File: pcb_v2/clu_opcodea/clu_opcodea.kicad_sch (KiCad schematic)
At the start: 45 parts, among them J1 UCODE, U1 74LS00

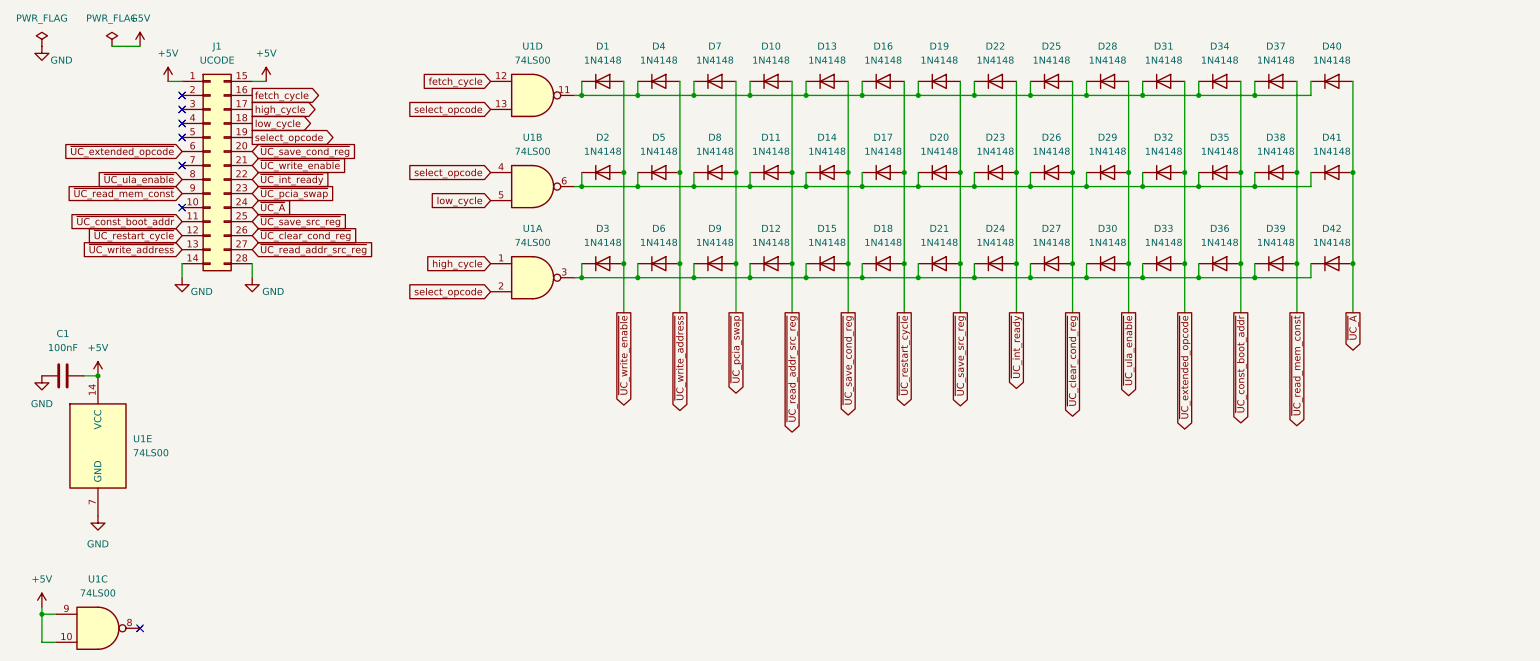
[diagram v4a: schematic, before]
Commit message: ajuste nos sinais do microcódigo
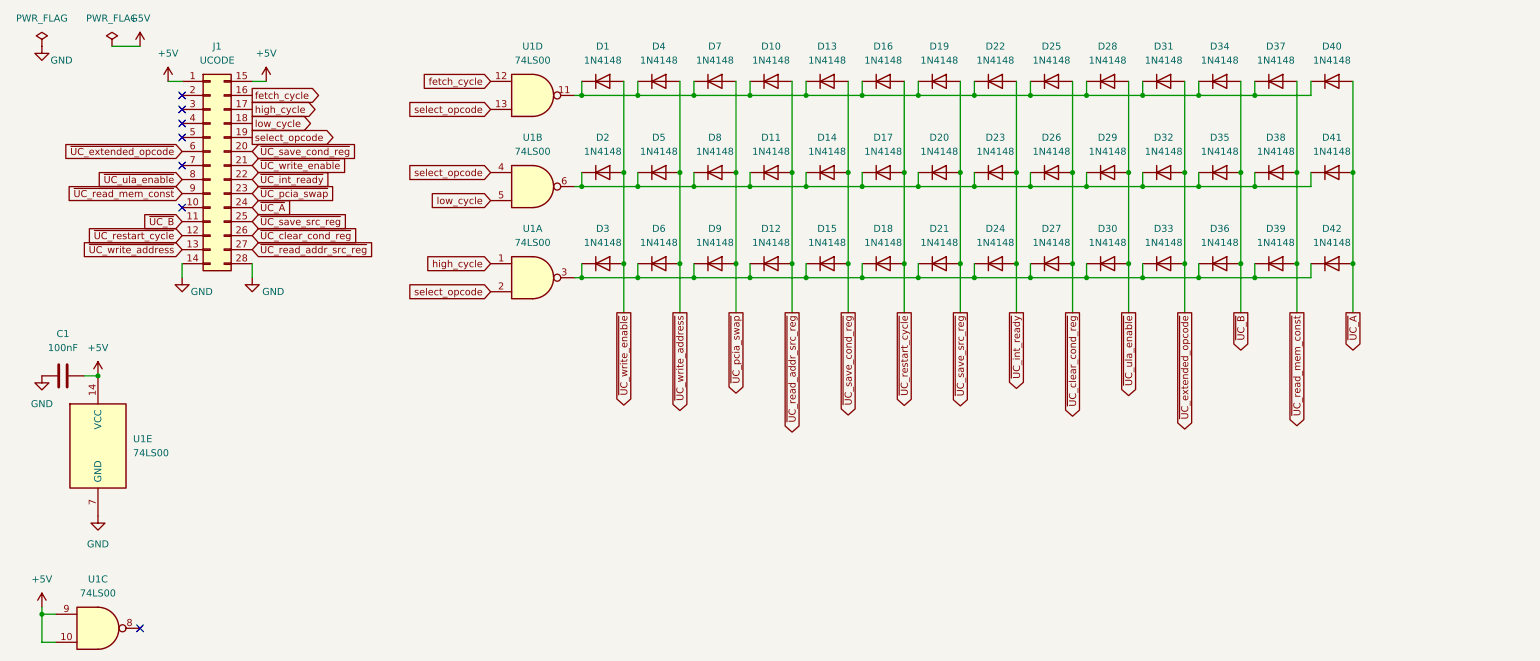
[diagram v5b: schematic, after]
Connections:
- net ~{UC_const_boot_addr} renamed ~{UC_B}
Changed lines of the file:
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@@
 		)
 	)
-	(global_label "~{UC_const_boot_addr}"
+	(global_label "~{UC_read_mem_const}"
+		(shape output)
+		(at 247.65 69.85 270)
+		(fields_autoplaced yes)
+		(effects
+			(font
+				(size 1.27 1.27)
+			)
+			(justify right)
+		)
+		(property "Intersheetrefs" "${INTERSHEET_REFS}"
+			(at 247.65 92.1269 90)
+			(effects
+				(font
+					(size 1.27 1.27)
+				)
+				(justify right)
+				(hide yes)
+			)
+		)
+	)
+	(global_label "~{UC_write_address}"
+		(shape output)
+		(at 135.89 69.85 270)
+		(fields_autoplaced yes)
+		(effects
+			(font
+				(size 1.27 1.27)
+			)
+			(justify right)
+		)
+		(property "Intersheetrefs" "${INTERSHEET_REFS}"
+			(at 135.89 89.2847 90)
+			(effects
+				(font
+					(size 1.27 1.27)
+				)
+				(justify right)
+				(hide yes)
+			)
+		)
+	)
+	(global_label "~{UC_clear_cond_reg}"
+		(shape input)
+		(at 58.42 55.88 0)
+		(fields_autoplaced yes)
+		(effects
+			(font
+				(size 1.27 1.27)
+			)
+			(justify left)
+		)
+		(property "Intersheetrefs" "${INTERSHEET_REFS}"
+			(at 79.2455 55.88 0)
+			(effects
+				(font
+					(size 1.27 1.27)
+				)
+				(justify left)
+				(hide yes)
+			)
+		)
+	)
+	(global_label "~{UC_extended_opcode}"
+		(shape input)
+		(at 45.72 40.64 180)
+		(fields_autoplaced yes)
+		(effects
+			(font
+				(size 1.27 1.27)
+			)
+			(justify right)
+		)
+		(property "Intersheetrefs" "${INTERSHEET_REFS}"
+			(at 22.9593 40.64 0)
+			(effects
+				(font
+					(size 1.27 1.27)
+				)
+				(justify right)
+				(hide yes)
+			)
+		)
+	)
+	(global_label "high_cycle"
+		(shape input)
+		(at 101.6 60.96 180)
+		(fields_autoplaced yes)
+		(effects
+			(font
+				(size 1.27 1.27)
+			)
+			(justify right)
+		)
+		(property "Intersheetrefs" "${INTERSHEET_REFS}"
+			(at 88.6968 60.96 0)
+			(effects
+				(font
+					(size 1.27 1.27)
+				)
+				(justify right)
+				(hide yes)
+			)
+		)
+	)
+	(global_label "~{UC_A}"
+		(shape input)
+		(at 58.42 50.8 0)
+		(fields_autoplaced yes)
+		(effects
+			(font
+				(size 1.27 1.27)
+			)
+			(justify left)
+		)
+		(property "Intersheetrefs" "${INTERSHEET_REFS}"
+			(at 66.0619 50.8 0)
+			(effects
+				(font
+					(size 1.27 1.27)
+				)
+				(justify left)
+				(hide yes)
+			)
+		)
+	)
+	(global_label "~{UC_pcia_swap}"
+		(shape input)
+		(at 58.42 48.26 0)
+		(fields_autoplaced yes)
+		(effects
+			(font
+				(size 1.27 1.27)
+			)
+			(justify left)
+		)
+		(property "Intersheetrefs" "${INTERSHEET_REFS}"
+			(at 74.5889 48.26 0)
+			(effects
+				(font
+					(size 1.27 1.27)
+				)
+				(justify left)
+				(hide yes)
+			)
+		)
+	)
+	(global_label "~{UC_B}"
+		(shape input)
+		(at 45.72 53.34 180)
+		(fields_autoplaced yes)
+		(effects
+			(font
+				(size 1.27 1.27)
+			)
+			(justify right)
+		)
+		(property "Intersheetrefs" "${INTERSHEET_REFS}"
+			(at 37.8967 53.34 0)
+			(effects
+				(font
+					(size 1.27 1.27)
+				)
+				(justify right)
+				(hide yes)
+			)
+		)
+	)
+	(global_label "~{UC_A}"
+		(shape output)
+		(at 257.81 69.85 270)
+		(fields_autoplaced yes)
+		(effects
+			(font
+				(size 1.27 1.27)
+			)
+			(justify right)
+		)
+		(property "Intersheetrefs" "${INTERSHEET_REFS}"
+			(at 257.81 77.4919 90)
+			(effects
+				(font
+					(size 1.27 1.27)
+				)
+				(justify right)
+				(hide yes)
+			)
+		)
+	)
+	(global_label "~{UC_int_ready}"
+		(shape output)
+		(at 196.85 69.85 270)
+		(fields_autoplaced yes)
+		(effects
+			(font
+				(size 1.27 1.27)
+			)
+			(justify right)
+		)
+		(property "Intersheetrefs" "${INTERSHEET_REFS}"
+			(at 196.85 84.9908 90)
+			(effects
+				(font
+					(size 1.27 1.27)
+				)
+				(justify right)
+				(hide yes)
+			)
+		)
+	)
+	(global_label "~{UC_extended_opcode}"
+		(shape output)
+		(at 227.33 69.85 270)
+		(fields_autoplaced yes)
+		(effects
+			(font
+				(size 1.27 1.27)
+			)
+			(justify right)
+		)
+		(property "Intersheetrefs" "${INTERSHEET_REFS}"
+			(at 227.33 92.6107 90)
+			(effects
+				(font
+					(size 1.27 1.27)
+				)
+				(justify right)
+				(hide yes)
+			)
+		)
+	)
+	(global_label "~{UC_B}"
 		(shape output)
 		(at 237.49 69.85 270)
@@
 		)
 		(property "Intersheetrefs" "${INTERSHEET_REFS}"
-			(at 237.49 91.8848 90)
-			(effects
-				(font
-					(size 1.27 1.27)
-				)
-				(justify right)
-				(hide yes)
-			)
-		)
-	)
-	(global_label "~{UC_read_mem_const}"
-		(shape output)
-		(at 247.65 69.85 270)
-		(fields_autoplaced yes)
-		(effects
-			(font
-				(size 1.27 1.27)
-			)
-			(justify right)
-		)
-		(property "Intersheetrefs" "${INTERSHEET_REFS}"
-			(at 247.65 92.1269 90)
-			(effects
-				(font
-					(size 1.27 1.27)
-				)
-				(justify right)
-				(hide yes)
-			)
-		)
-	)
-	(global_label "~{UC_write_address}"
-		(shape output)
-		(at 135.89 69.85 270)
-		(fields_autoplaced yes)
-		(effects
-			(font
-				(size 1.27 1.27)
-			)
-			(justify right)
-		)
-		(property "Intersheetrefs" "${INTERSHEET_REFS}"
-			(at 135.89 89.2847 90)
-			(effects
-				(font
-					(size 1.27 1.27)
-				)
-				(justify right)
-				(hide yes)
-			)
-		)
-	)
-	(global_label "~{UC_clear_cond_reg}"
-		(shape input)
-		(at 58.42 55.88 0)
-		(fields_autoplaced yes)
-		(effects
-			(font
-				(size 1.27 1.27)
-			)
-			(justify left)
-		)
-		(property "Intersheetrefs" "${INTERSHEET_REFS}"
-			(at 79.2455 55.88 0)
-			(effects
-				(font
-					(size 1.27 1.27)
-				)
-				(justify left)
-				(hide yes)
-			)
-		)
-	)
-	(global_label "~{UC_extended_opcode}"
-		(shape input)
-		(at 45.72 40.64 180)
-		(fields_autoplaced yes)
-		(effects
-			(font
-				(size 1.27 1.27)
-			)
-			(justify right)
-		)
-		(property "Intersheetrefs" "${INTERSHEET_REFS}"
-			(at 22.9593 40.64 0)
-			(effects
-				(font
-					(size 1.27 1.27)
-				)
-				(justify right)
-				(hide yes)
-			)
-		)
-	)
-	(global_label "high_cycle"
-		(shape input)
-		(at 101.6 60.96 180)
-		(fields_autoplaced yes)
-		(effects
-			(font
-				(size 1.27 1.27)
-			)
-			(justify right)
-		)
-		(property "Intersheetrefs" "${INTERSHEET_REFS}"
-			(at 88.6968 60.96 0)
-			(effects
-				(font
-					(size 1.27 1.27)
-				)
-				(justify right)
-				(hide yes)
-			)
-		)
-	)
-	(global_label "~{UC_A}"
-		(shape input)
-		(at 58.42 50.8 0)
-		(fields_autoplaced yes)
-		(effects
-			(font
-				(size 1.27 1.27)
-			)
-			(justify left)
-		)
-		(property "Intersheetrefs" "${INTERSHEET_REFS}"
-			(at 66.0619 50.8 0)
-			(effects
-				(font
-					(size 1.27 1.27)
-				)
-				(justify left)
-				(hide yes)
-			)
-		)
-	)
-	(global_label "~{UC_pcia_swap}"
-		(shape input)
-		(at 58.42 48.26 0)
-		(fields_autoplaced yes)
-		(effects
-			(font
-				(size 1.27 1.27)
-			)
-			(justify left)
-		)
-		(property "Intersheetrefs" "${INTERSHEET_REFS}"
-			(at 74.5889 48.26 0)
-			(effects
-				(font
-					(size 1.27 1.27)
-				)
-				(justify left)
-				(hide yes)
-			)
-		)
-	)
-	(global_label "~{UC_A}"
-		(shape output)
-		(at 257.81 69.85 270)
-		(fields_autoplaced yes)
-		(effects
-			(font
-				(size 1.27 1.27)
-			)
-			(justify right)
-		)
-		(property "Intersheetrefs" "${INTERSHEET_REFS}"
-			(at 257.81 77.4919 90)
-			(effects
-				(font
-					(size 1.27 1.27)
-				)
-				(justify right)
-				(hide yes)
-			)
-		)
-	)
-	(global_label "~{UC_int_ready}"
-		(shape output)
-		(at 196.85 69.85 270)
-		(fields_autoplaced yes)
-		(effects
-			(font
-				(size 1.27 1.27)
-			)
-			(justify right)
-		)
-		(property "Intersheetrefs" "${INTERSHEET_REFS}"
-			(at 196.85 84.9908 90)
-			(effects
-				(font
-					(size 1.27 1.27)
-				)
-				(justify right)
-				(hide yes)
-			)
-		)
-	)
-	(global_label "~{UC_extended_opcode}"
-		(shape output)
-		(at 227.33 69.85 270)
-		(fields_autoplaced yes)
-		(effects
-			(font
-				(size 1.27 1.27)
-			)
-			(justify right)
-		)
-		(property "Intersheetrefs" "${INTERSHEET_REFS}"
-			(at 227.33 92.6107 90)
-			(effects
-				(font
-					(size 1.27 1.27)
-				)
-				(justify right)
-				(hide yes)
-			)
-		)
-	)
-	(global_label "~{UC_const_boot_addr}"
-		(shape input)
-		(at 45.72 53.34 180)
-		(fields_autoplaced yes)
-		(effects
-			(font
-				(size 1.27 1.27)
-			)
-			(justify right)
-		)
-		(property "Intersheetrefs" "${INTERSHEET_REFS}"
-			(at 23.6852 53.34 0)
-			(effects
-				(font
+			(at 237.49 77.6733 90)
+			(effects
+				(font

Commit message: novo sinal no opcode
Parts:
- removed U1: 74LS00, Package_DIP:DIP-14_W7.62mm, symbol 74xx:74LS00
- added U1: 74LS32, Package_DIP:DIP-14_W7.62mm, symbol 74xx:74LS32
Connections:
- net +5V: now also U1.10, U1.14 (VCC), U1.9
- net GND: now also U1.7 (GND)
- net fetch_cycle: now also U1.12
- net high_cycle: now also U1.1
- net low_cycle: now also U1.5
- net select_opcode: now also U1.13, U1.2, U1.4
- net at D12.1 (K), D15.1 (K), D18.1 (K)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: now also U1.3
- net at D11.1 (K), D14.1 (K), D17.1 (K)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: now also U1.6
- net at D1.1 (K), D10.1 (K), D13.1 (K)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: now also U1.11
- net ~{UC_B} renamed ~{UC_disable_int}
